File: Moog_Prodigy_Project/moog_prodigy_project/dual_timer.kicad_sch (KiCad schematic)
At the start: 3 parts, among them U77 NE556N

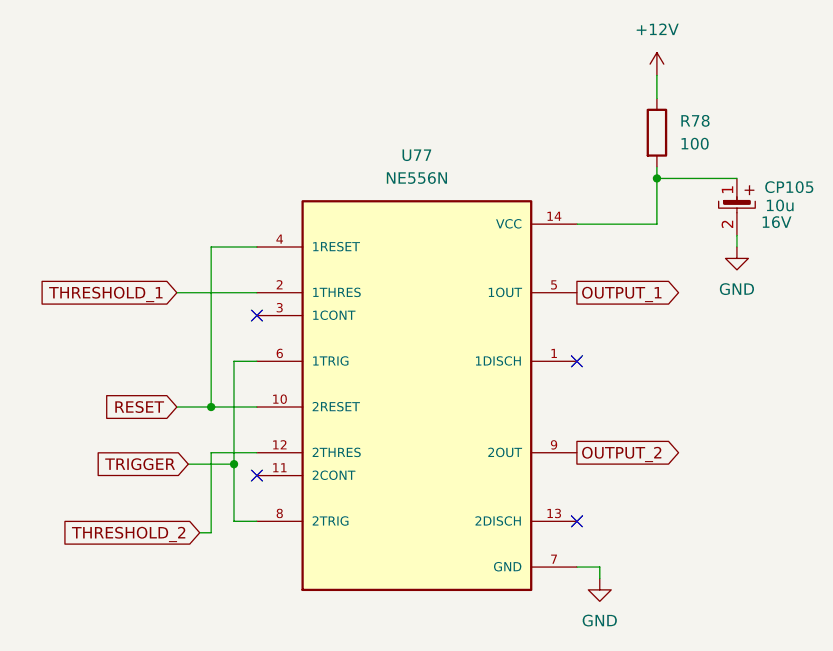
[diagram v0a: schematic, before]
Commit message: problemi sa ca3096, multiplicirani footprintovi
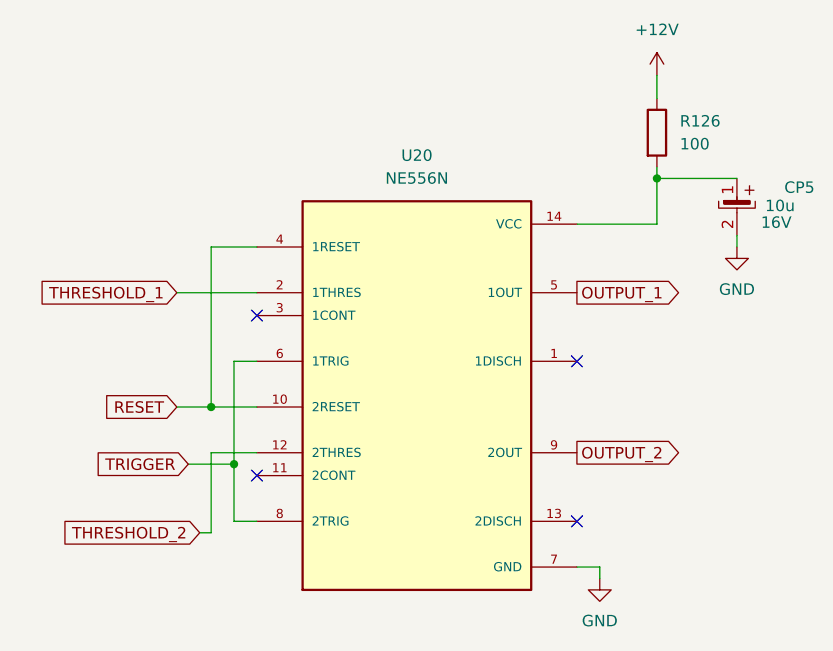
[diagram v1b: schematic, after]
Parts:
- renumbered CP105 to CP5, R78 to R126, U77 to U20
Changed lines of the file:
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@@
 		(dnp no)
 		(fields_autoplaced yes)
-		(property "Reference" "R78"
+		(property "Reference" "R126"
 			(at 189.23 49.5299 0)
 			(effects
@@
 			(project "moog_prodigy_project"
 				(path "/db469bdb-b6c3-4a16-9199-d4e6b8d556e8/3db0e499-9ab2-4148-8bd3-6413362a052c"
-					(reference "R78")
+					(reference "R126")
 					(unit 1)
 				)
@@
 		(on_board yes)
 		(dnp no)
-		(property "Reference" "CP105"
+		(property "Reference" "CP5"
 			(at 204.216 56.896 0)
 			(effects
@@
 			(project "moog_prodigy_project"
 				(path "/db469bdb-b6c3-4a16-9199-d4e6b8d556e8/3db0e499-9ab2-4148-8bd3-6413362a052c"
-					(reference "CP105")
+					(reference "CP5")
 					(unit 1)
 				)
@@
 		(dnp no)
 		(fields_autoplaced yes)
-		(property "Reference" "#PWR029"
+		(property "Reference" "#PWR0153"
 			(at 195.58 69.85 0)
 			(effects
@@
 			(project "moog_prodigy_project"
 				(path "/db469bdb-b6c3-4a16-9199-d4e6b8d556e8/3db0e499-9ab2-4148-8bd3-6413362a052c"
-					(reference "#PWR029")
+					(reference "#PWR0153")
 					(unit 1)
 				)
@@
 		(dnp no)
 		(fields_autoplaced yes)
-		(property "Reference" "U77"
+		(property "Reference" "U20"
 			(at 160.02 53.34 0)
 			(effects
@@
 			(project "moog_prodigy_project"
 				(path "/db469bdb-b6c3-4a16-9199-d4e6b8d556e8/3db0e499-9ab2-4148-8bd3-6413362a052c"
-					(reference "U77")
+					(reference "U20")
 					(unit 1)
 				)
@@
 		(dnp no)
 		(fields_autoplaced yes)
-		(property "Reference" "#PWR028"
+		(property "Reference" "#PWR0152"
 			(at 186.69 48.26 0)
 			(effects
@@
 			(project "moog_prodigy_project"
 				(path "/db469bdb-b6c3-4a16-9199-d4e6b8d556e8/3db0e499-9ab2-4148-8bd3-6413362a052c"
-					(reference "#PWR028")
+					(reference "#PWR0152")
 					(unit 1)
 				)
@@
 		(dnp no)
 		(fields_autoplaced yes)
-		(property "Reference" "#PWR027"
+		(property "Reference" "#PWR0151"
 			(at 180.34 106.68 0)
 			(effects
@@
 			(project "moog_prodigy_project"
 				(path "/db469bdb-b6c3-4a16-9199-d4e6b8d556e8/3db0e499-9ab2-4148-8bd3-6413362a052c"
-					(reference "#PWR027")
+					(reference "#PWR0151")
 					(unit 1)
 				)

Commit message: Latest checkpoints update 05.06.2026
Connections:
- net GND: now also CP5.; no longer CP5.2
- net at R126.2, U20.14 (VCC): now also CP5.; no longer CP5.1
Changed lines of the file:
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@@
+	(wire
+		(pts
+			(xy 195.58 55.88) (xy 195.58 57.15)
+		)
+		(stroke
+			(width 0)
+			(type default)
+		)
+	)
 	(wire
 		(pts
@@
 	(wire
 		(pts
-			(xy 195.58 62.23) (xy 195.58 63.5)
-		)
-		(stroke
-			(width 0)
-			(type default)
-		)
-	)
-	(wire
-		(pts
-			(xy 186.69 60.96) (xy 186.69 55.88)
+			(xy 186.69 54.61) (xy 186.69 55.88)
+		)
+		(stroke
+			(width 0)
+			(type default)
+		)
+	)
+	(wire
+		(pts
+			(xy 186.69 55.88) (xy 186.69 60.96)
 		)
 		(stroke
@@
 		(pts
 			(xy 186.69 55.88) (xy 195.58 55.88)
-		)
-		(stroke
-			(width 0)
-			(type default)
-		)
-	)
-	(wire
-		(pts
-			(xy 186.69 54.61) (xy 186.69 55.88)
 		)
 		(stroke
@@
 		(on_board yes)
 		(dnp no)
-		(fields_autoplaced yes)
 		(property "Reference" "R126"
-			(at 189.23 49.5299 0)
+			(at 188.468 49.7839 0)
 			(effects
 				(font
@@
 		)
 		(property "Value" "100"
-			(at 189.23 52.0699 0)
+			(at 188.976 51.816 0)
 			(effects
 				(font
@@
 		(lib_name "elektrolit_3")
 		(lib_id "elektrolitski:elektrolit")
-		(at 195.58 58.42 0)
+		(at 195.58 59.69 0)
 		(unit 1)
 		(exclude_from_sim no)
@@
 		(dnp no)
 		(property "Reference" "CP5"
-			(at 204.216 56.896 0)
+			(at 192.786 59.182 0)
 			(effects
 				(font
@@
 		)
 		(property "Value" "10u"
-			(at 202.0316 58.928 0)
+			(at 202.0316 60.198 0)
 			(effects
 				(font
@@
 		)
 		(property "Footprint" "Capacitor_THT:CP_Radial_D5.0mm_P2.50mm"
-			(at 195.58 69.85 0)
+			(at 195.58 71.12 0)
 			(effects
 				(font
@@
 		)
 		(property "Datasheet" ""
-			(at 195.326 58.42 0)
+			(at 195.326 59.69 0)
 			(effects
 				(font
@@
 		)
 		(property "Description" ""
-			(at 195.58 58.42 0)
+			(at 195.58 59.69 0)
 			(effects
 				(font
@@
 		)
 		(property "Rated Voltage" "16V"
-			(at 199.9488 60.7822 0)
-			(effects
-				(font
-					(size 1.27 1.27)
-				)
-			)
-		)
-		(pin "1"
-		)
-		(pin "2"
+			(at 200.152 62.23 0)
+			(effects
+				(font
+					(size 1.27 1.27)
+				)
+			)
+		)
+		(pin ""
+		)
+		(pin ""
 		)
 		(instances
